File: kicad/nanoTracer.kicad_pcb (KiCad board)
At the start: 2 copper layers, 91.4 x 59.9 mm, 45 parts, among them J1 SIL10, P1 6.3_AC, P2 HEATER, P3 CONN_3, P4 HT_AC, P5 NEG_AC, U1 TL072, U2 TL071, U3 MCP4921-E/P, U4 LM337T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

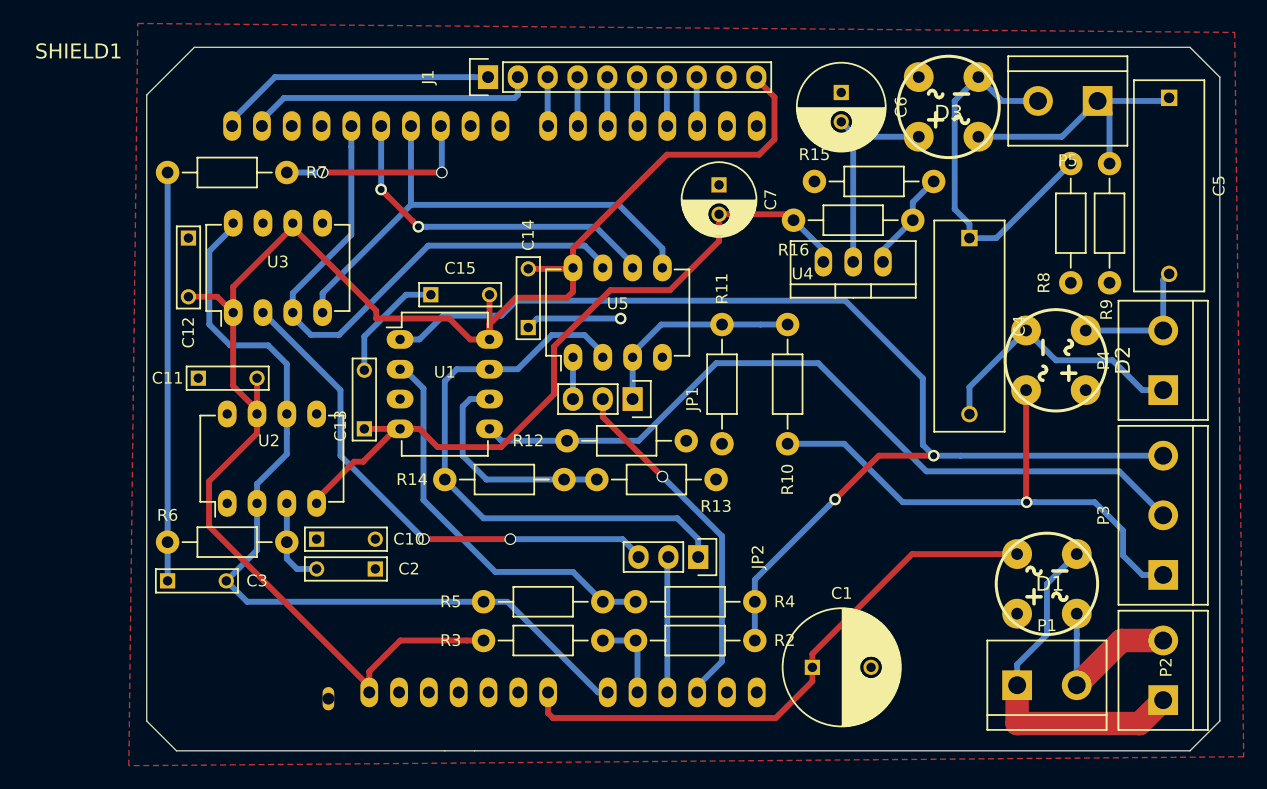
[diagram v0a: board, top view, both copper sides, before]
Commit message: Fix diode bridges footprints in PCB
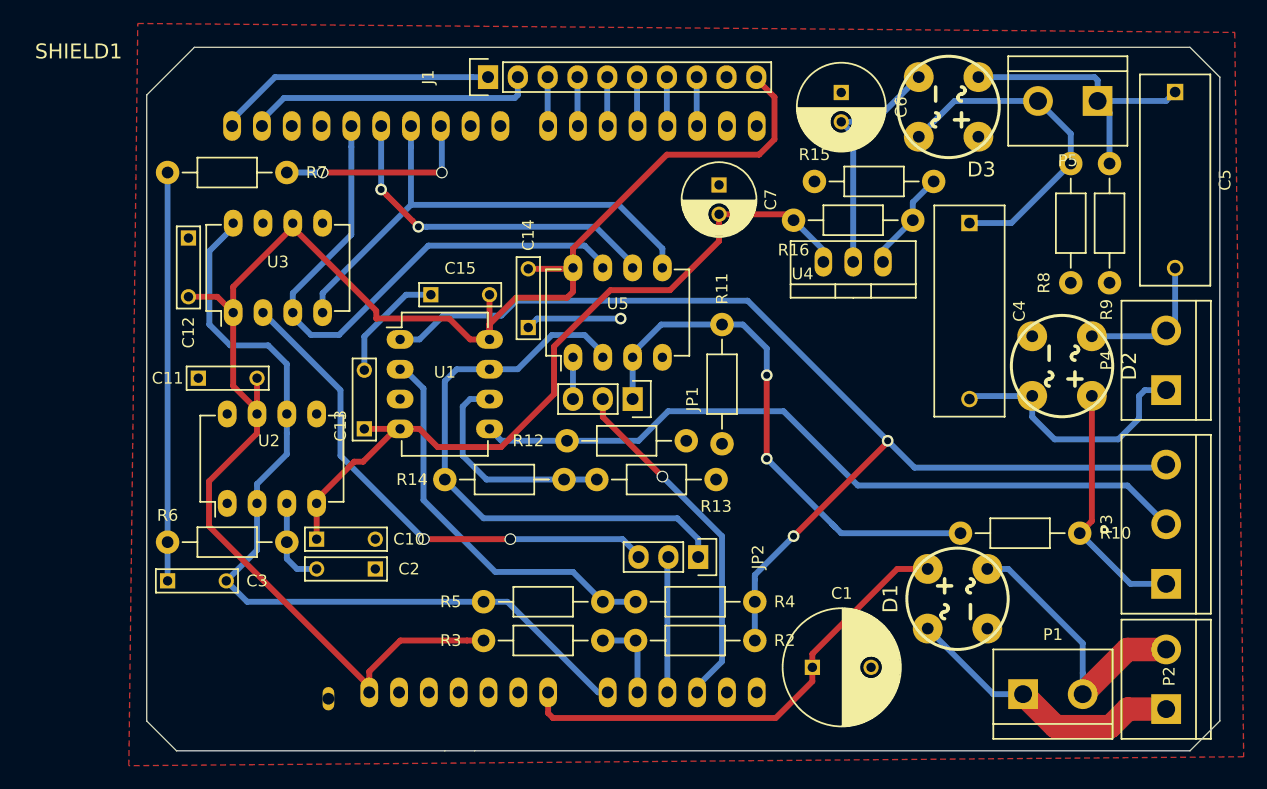
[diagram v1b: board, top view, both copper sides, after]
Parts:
- moved R10 26.0 mm to (239.5, 88.9), turned to 180 degrees
- moved D1 7.73 mm to (229.1, 94.5), turned to 270 degrees
- moved C4 1.28 mm to (230.1, 62.5)
- moved P1 0.92 mm to (237.2, 102.6)
- moved P2 0.80 mm to (246.9, 101.3)
- moved P3 0.80 mm to (246.9, 88.1)
- moved D2 0.72 mm to (238.0, 74.7)
- moved C5 0.71 mm to (247.7, 51.3)
- moved P4 0.25 mm to (246.9, 74.2)
- turned D3 to 90 degrees
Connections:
- D1 pad 4: Net-(D1-Pad2) -> Net-(D1-Pad4)
- P1 pad 2: Net-(P1-Pad2) -> Net-(D1-Pad4)
- P2 pad 2: Net-(P1-Pad2) -> Net-(D1-Pad4)
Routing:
- net /UA: track 18.1 -> 46.1 mm, vias 0 -> 2
- net A+: track 47.5 -> 21.3 mm, vias 1 -> 0
- net Net-(D1-Pad4): track 0.00 -> 23.8 mm
- net Net-(P1-Pad2): track 13.2 -> 0.00 mm
- net /VIN: track 49.1 -> 40.9 mm
- net Net-(D1-Pad2): track 31.6 -> 24.4 mm
- net /GRID: track 100.0 -> 95.1 mm
- net Net-(C4-Pad1): track 32.3 -> 28.6 mm
- net VSS: track 63.9 -> 67.0 mm
- net /UK: track 65.9 -> 63.1 mm
- net Net-(C6-Pad2): track 18.1 -> 20.5 mm
- net Net-(C5-Pad2): track 11.6 -> 13.2 mm
- net Net-(C5-Pad1): track 23.4 -> 24.0 mm

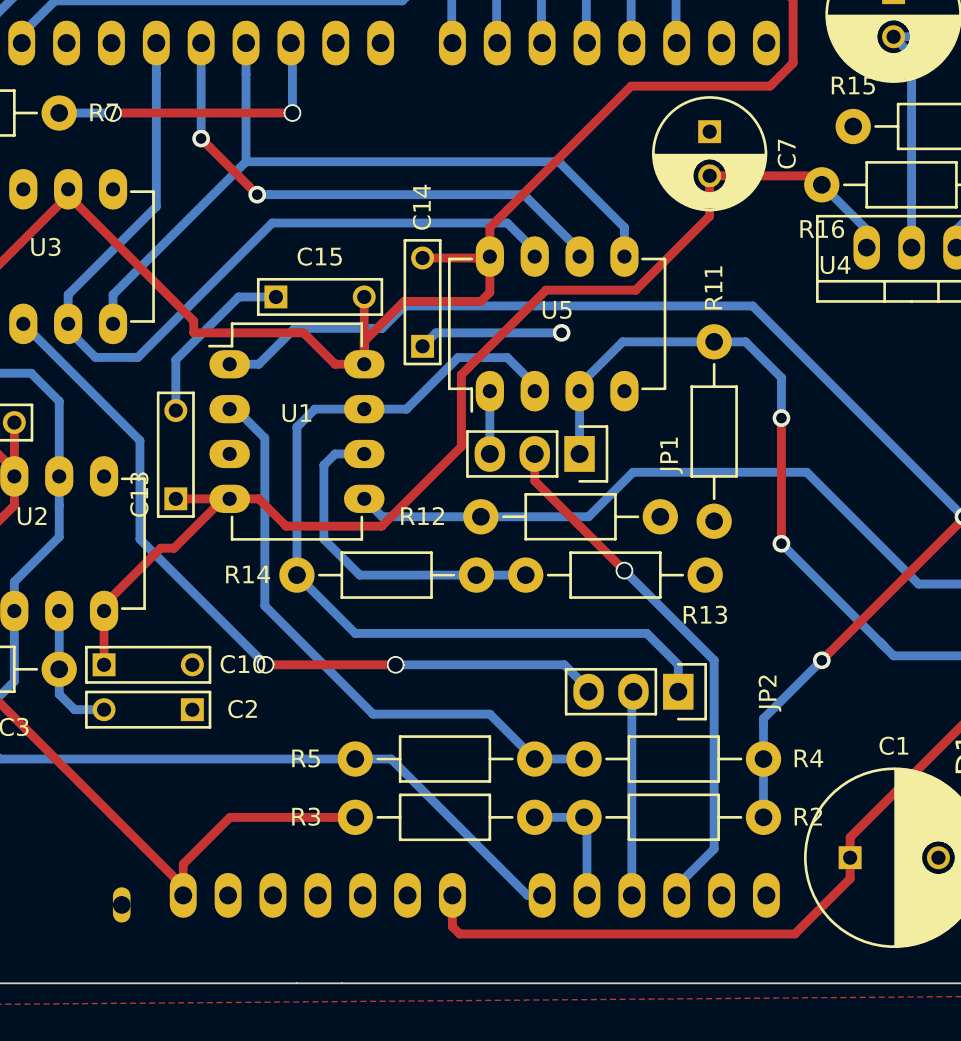
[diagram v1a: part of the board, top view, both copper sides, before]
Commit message: Fix vias diameter & remove unused pin
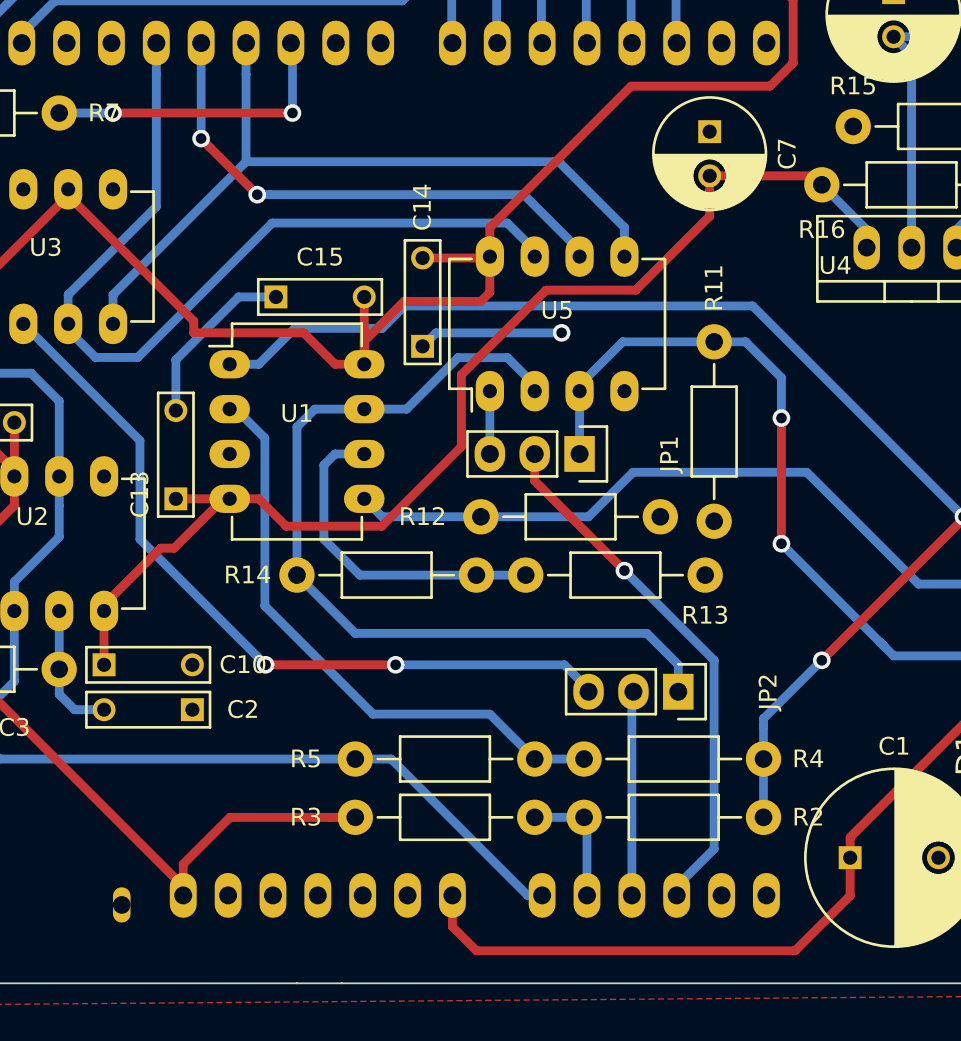
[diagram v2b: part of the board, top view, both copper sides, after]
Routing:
- net /VIN: track 40.9 -> 42.3 mm
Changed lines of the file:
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@@
     (visible_elements FFFFEF7F)
     (pcbplotparams
-      (layerselection 0x20020_80000001)
+      (layerselection 0x210e0_80000001)
       (usegerberextensions false)
       (excludeedgelayer true)
@@
   (gr_line (start 164.084 47.498) (end 248.92 47.498) (layer Edge.Cuts) (width 0.1))
   (gr_line (start 160.02 51.562) (end 164.084 47.498) (layer Edge.Cuts) (width 0.1))
+  (segment (start 194.2211 102.4636) (end 194.2211 104.2336) (width 0.5) (layer F.Cu) (net 1))
+  (segment (start 194.2211 104.2336) (end 195.583835 105.596335) (width 0.5) (layer F.Cu) (net 1))
+  (segment (start 195.583835 105.596335) (end 213.628554 105.596335) (width 0.5) (layer F.Cu) (net 1))
+  (segment (start 213.628554 105.596335) (end 216.742 102.482889) (width 0.5) (layer F.Cu) (net 1))
+  (segment (start 216.742 102.482889) (end 216.742 100.33) (width 0.5) (layer F.Cu) (net 1))
   (segment (start 223.974 91.948) (end 226.568 91.948) (width 0.5) (layer F.Cu) (net 1))
   (segment (start 216.742 100.33) (end 216.742 99.18) (width 0.5) (layer F.Cu) (net 1))
   (segment (start 216.742 99.18) (end 223.974 91.948) (width 0.5) (layer F.Cu) (net 1))
-  (segment (start 213.614 104.648) (end 216.742 101.52) (width 0.5) (layer F.Cu) (net 1))
-  (segment (start 216.742 101.52) (end 216.742 100.33) (width 0.5) (layer F.Cu) (net 1))
-  (segment (start 194.6355 104.648) (end 213.614 104.648) (width 0.5) (layer F.Cu) (net 1))
-  (segment (start 194.2211 102.4636) (end 194.2211 104.2336) (width 0.5) (layer F.Cu) (net 1))
-  (segment (start 194.2211 104.2336) (end 194.6355 104.648) (width 0.5) (layer F.Cu) (net 1))
   (segment (start 178.562 72.136) (end 182.118 68.58) (width 0.5) (layer B.Cu) (net 2))
   (segment (start 193.294 70.612) (end 200.406 70.612) (width 0.5) (layer B.Cu) (net 2))
@@
   (segment (start 198.882 77.47) (end 198.882 78.994) (width 0.5) (layer F.Cu) (net 16))
   (segment (start 198.882 78.994) (end 203.962 84.074) (width 0.5) (layer F.Cu) (net 16))
-  (via (at 203.962 84.074) (size 1) (drill 0.8) (layers F.Cu B.Cu) (net 16))
+  (via (at 203.962 84.074) (size 1) (drill 0.6) (layers F.Cu B.Cu) (net 16))
   (segment (start 196.342 77.47) (end 196.342 73.914) (width 0.5) (layer B.Cu) (net 17))
   (segment (start 189.23 74.93) (end 191.626002 74.93) (width 0.5) (layer B.Cu) (net 18))
@@
   (segment (start 200.5584 89.408) (end 201.93 90.7796) (width 0.5) (layer B.Cu) (net 20))
   (segment (start 201.93 90.7796) (end 201.93 90.932) (width 0.5) (layer B.Cu) (net 20))
-  (via (at 191.008 89.408) (size 1) (drill 0.8) (layers F.Cu B.Cu) (net 20))
+  (via (at 191.008 89.408) (size 1) (drill 0.6) (layers F.Cu B.Cu) (net 20))
   (segment (start 183.642 89.408) (end 191.008 89.408) (width 0.5) (layer F.Cu) (net 20))
   (segment (start 176.53 82.296) (end 183.642 89.408) (width 0.5) (layer B.Cu) (net 20))
-  (via (at 183.642 89.408) (size 1) (drill 0.8) (layers F.Cu B.Cu) (net 20))
+  (via (at 183.642 89.408) (size 1) (drill 0.6) (layers F.Cu B.Cu) (net 20))
   (segment (start 176.53 76.710045) (end 176.53 82.296) (width 0.5) (layer B.Cu) (net 20))
   (segment (start 169.926 70.104) (end 169.926 70.106045) (width 0.5) (layer B.Cu) (net 20))
@@
   (segment (start 185.166 58.166) (end 185.166 54.2925) (width 0.5) (layer B.Cu) (net 25))
   (segment (start 185.166 54.2925) (end 185.0771 54.2036) (width 0.5) (layer B.Cu) (net 25))
-  (via (at 185.166 58.166) (size 1) (drill 0.8) (layers F.Cu B.Cu) (net 25))
+  (via (at 185.166 58.166) (size 1) (drill 0.6) (layers F.Cu B.Cu) (net 25))
   (segment (start 171.958 58.166) (end 175.006 58.166) (width 0.5) (layer B.Cu) (net 25))
-  (via (at 175.006 58.166) (size 1) (drill 0.8) (layers F.Cu B.Cu) (net 25))
+  (via (at 175.006 58.166) (size 1) (drill 0.6) (layers F.Cu B.Cu) (net 25))
   (segment (start 185.0771 54.2036) (end 185.0771 54.097295) (width 0.5) (layer B.Cu) (net 25))
   (segment (start 195.58 84.328) (end 198.374 84.328) (width 0.5) (layer B.Cu) (net 26))

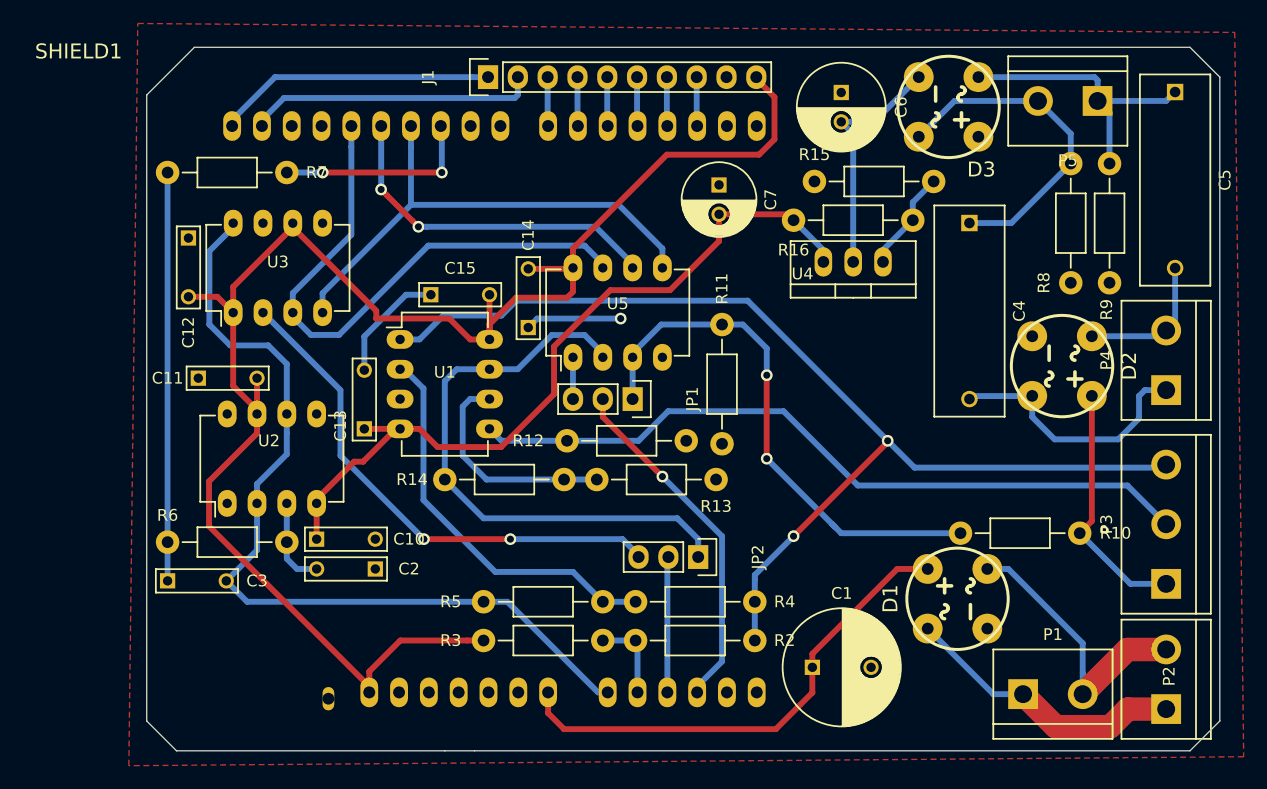
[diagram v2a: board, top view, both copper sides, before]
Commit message: Optimize routing & silkscreen
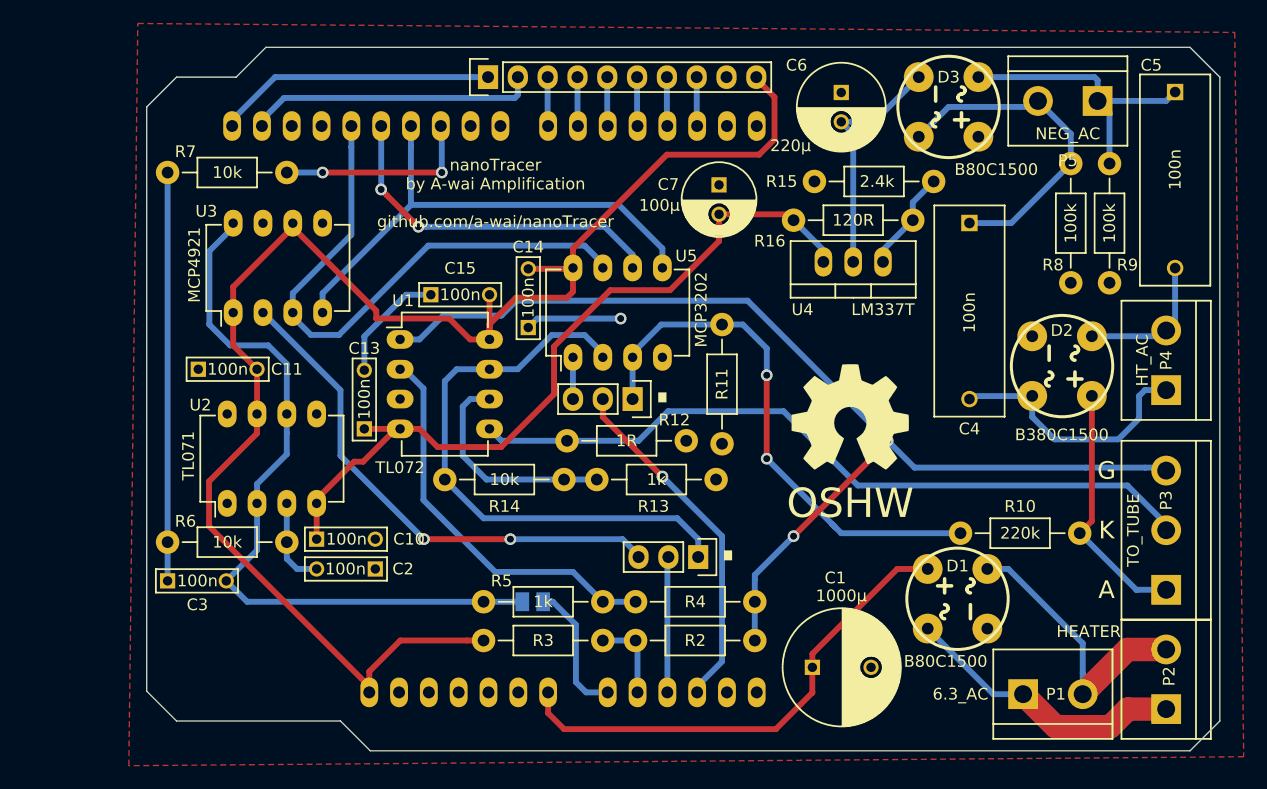
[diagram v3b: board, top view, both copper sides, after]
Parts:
- removed C12: 100n, Capacitors_ThroughHole:C_Rect_L7_W2_P5
- added JP3: JUMPER, freetronics_footprints:SJ_OPEN, F.Cu at (192.8, 94.7)
- added LOGO_OSHW_silkscreen_10mm: val**, freetronics_footprints:LOGO_OSHW_silkscreen_10mm, F.Cu at (220.0, 79.0)
- P3: value CONN_3 -> TO_TUBE
- U3: value MCP4921-E/P -> MCP4921
- moved C11 0.76 mm to (164.4, 74.9)
- moved P3 0.51 mm to (246.9, 88.6)
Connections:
- SHIELD1 pad AD0: /DAC_OUT -> Net-(JP3-Pad2)
- SHIELD1 pad GND3: Net-(SHIELD1-PadGND3) -> GND
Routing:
- net Net-(JP3-Pad2): track 0.00 -> 11.6 mm
- net /DAC_OUT: track 74.5 -> 64.1 mm
- net VDD: track 139.3 -> 132.2 mm
- net A+: track 21.3 -> 22.2 mm
- net /UK: track 63.1 -> 63.6 mm
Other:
- outline, holes or cut-outs redrawn
- board text added: "."
- board text added: "A"
- board text added: "G"
- board text added: "K"
- board text added: "OSHW"
- board text added: "nanoTracer by A-wai Amplification github.com/a-wai/nanoTracer"

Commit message: Added headers for unconnected Arduino pins
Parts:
- added P6: CONN_2, Pin_Headers:Pin_Header_Straight_1x02, F.Cu at (215.6, 94.7)
- added P7: CONN_2, Pin_Headers:Pin_Header_Straight_1x02, F.Cu at (188.2, 58.2)
- U3: value MCP4921 -> MCP4921-E/P
- moved C1 2.68 mm to (218.9, 101.9)
- moved LOGO_OSHW_silkscreen_10mm 0.76 mm to (220.0, 78.2)
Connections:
- SHIELD1 pad 0: Net-(SHIELD1-Pad0) -> (no net)
- SHIELD1 pad 1: Net-(SHIELD1-Pad1) -> (no net)
- SHIELD1 pad 3V3: Net-(SHIELD1-Pad3V3) -> (no net)
- SHIELD1 pad 5V: Net-(SHIELD1-Pad5V) -> (no net)
- SHIELD1 pad 8: Net-(SHIELD1-Pad8) -> /D8
- SHIELD1 pad 9: Net-(SHIELD1-Pad9) -> /D9
- SHIELD1 pad AREF: Net-(SHIELD1-PadAREF) -> (no net)
- SHIELD1 pad RST: Net-(SHIELD1-PadRST) -> (no net)
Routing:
- net Net-(P6-Pad1): track 0.00 -> 11.3 mm
- net Net-(P6-Pad2): track 0.00 -> 11.0 mm
- net /D9: track 0.00 -> 4.21 mm
- net /D8: track 0.00 -> 4.21 mm
